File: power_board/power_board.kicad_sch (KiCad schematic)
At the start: 0 parts

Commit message: Added test point
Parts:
- added TP1: Test_Point, symbol URC:Test_Point
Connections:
- new net GND: TP1.1
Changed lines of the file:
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@@
 (kicad_sch (version 20230121) (generator eeschema)
   (paper "A4")
+  (wire (pts (xy 40.64 165.1) (xy 40.64 171.45))
+    (stroke (width 0) (type default))
+  )
+  (symbol (lib_id "URC:GND") (at 40.64 171.45 0) (unit 1)
+    (in_bom yes) (on_board yes) (dnp no) (fields_autoplaced)
+    (property "Reference" "#PWR01" (at 40.64 177.8 0)
+      (effects (font (size 1.27 1.27)) hide)
+    )
+    (property "Value" "GND" (at 40.64 176.53 0)
+      (effects (font (size 1.27 1.27)))
+    )
+    (property "Footprint" "" (at 40.64 171.45 0)
+      (effects (font (size 1.27 1.27)) hide)
+    )
+    (property "Datasheet" "" (at 40.64 171.45 0)
+      (effects (font (size 1.27 1.27)) hide)
+    )
+    (pin "1")
+    (instances
+      (project "power_board"
+        (path "/8fb9e798-2690-4afb-a1e7-64efc74d0eca"
+          (reference "#PWR01") (unit 1)
+        )
+      )
+    )
+  )
+  (symbol (lib_id "URC:Test_Point") (at 40.64 165.1 0) (unit 1)
+    (in_bom yes) (on_board yes) (dnp no) (fields_autoplaced)
+    (property "Reference" "TP1" (at 43.18 160.528 0)
+      (effects (font (size 1.27 1.27)) (justify left))
+    )
+    (property "Value" "Test_Point" (at 43.18 163.068 0)
+      (effects (font (size 1.27 1.27)) (justify left))
+    )
+    (property "Footprint" "" (at 45.72 165.1 0)
+      (effects (font (size 1.27 1.27)) hide)
+    )
+    (property "Datasheet" "~" (at 45.72 165.1 0)
+      (effects (font (size 1.27 1.27)) hide)
+    )
+    (pin "1")
+    (instances
+      (project "power_board"
+        (path "/8fb9e798-2690-4afb-a1e7-64efc74d0eca"
+          (reference "TP1") (unit 1)
+        )
+      )
+    )
+  )
   (sheet_instances
     (path "/" (page "1"))

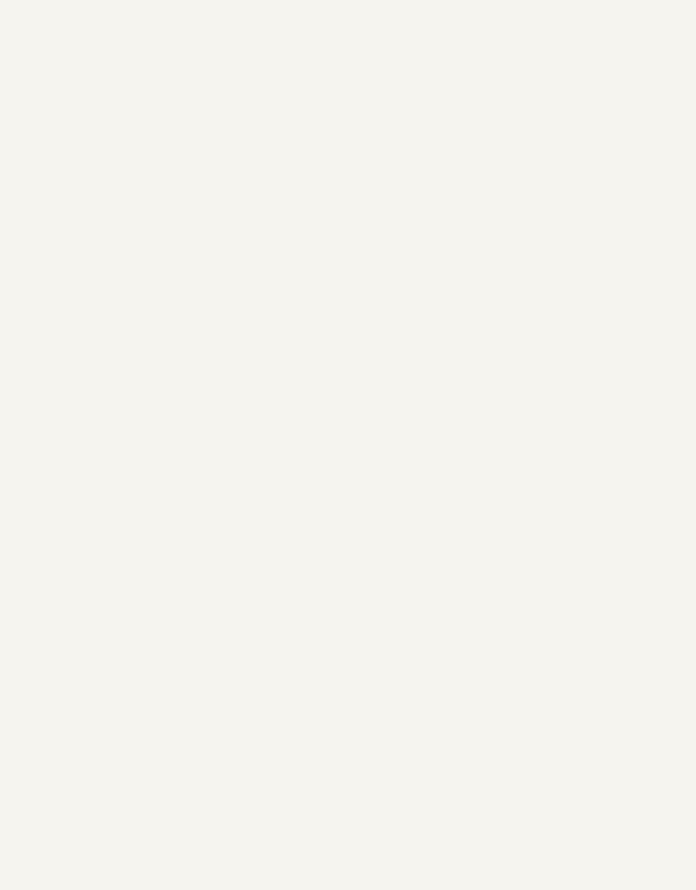
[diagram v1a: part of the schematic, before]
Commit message: Modified LCD Display symbol, added Arduino and LCD Display to schematic
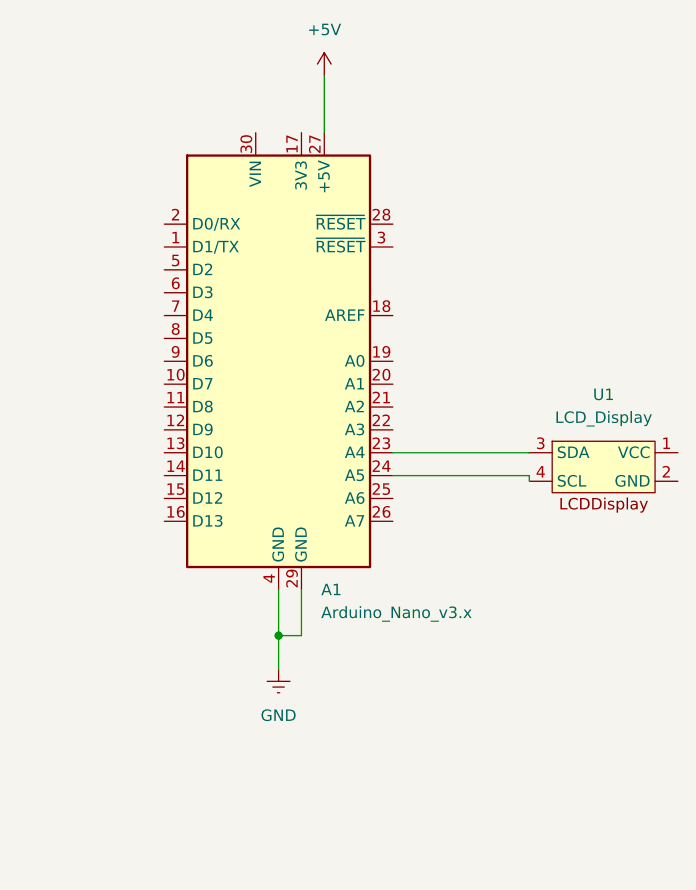
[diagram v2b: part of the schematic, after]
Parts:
- added A1: Arduino_Nano_v3.x, Module:Arduino_Nano, symbol URC:Arduino_Nano_v3.x
- added U1: LCD_Display, symbol URC:LCD_Display
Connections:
- net GND: now also A1.29 (GND), A1.4 (GND)
- new net: A1.23 (A4), U1.3 (SDA)
- new net: A1.24 (A5), U1.4 (SCL)
- new net +5V: A1.27 (+5V)
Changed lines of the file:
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@@
 (kicad_sch (version 20230121) (generator eeschema)
   (paper "A4")
+  (junction (at 142.24 104.14) (diameter 0) (color 0 0 0 0)
+  )
+  (wire (pts (xy 142.24 104.14) (xy 142.24 107.95))
+    (stroke (width 0) (type default))
+  )
+  (wire (pts (xy 170.1009 83.82) (xy 170.1009 83.815))
+    (stroke (width 0) (type default))
+  )
+  (wire (pts (xy 154.94 83.82) (xy 170.1009 83.82))
+    (stroke (width 0) (type default))
+  )
+  (wire (pts (xy 147.32 41.91) (xy 147.32 48.26))
+    (stroke (width 0) (type default))
+  )
+  (wire (pts (xy 170.1009 86.36) (xy 170.1009 86.99))
+    (stroke (width 0) (type default))
+  )
   (wire (pts (xy 40.64 165.1) (xy 40.64 171.45))
     (stroke (width 0) (type default))
   )
+  (wire (pts (xy 142.24 104.14) (xy 144.78 104.14))
+    (stroke (width 0) (type default))
+  )
+  (wire (pts (xy 142.24 99.06) (xy 142.24 104.14))
+    (stroke (width 0) (type default))
+  )
+  (wire (pts (xy 144.78 99.06) (xy 144.78 104.14))
+    (stroke (width 0) (type default))
+  )
+  (wire (pts (xy 154.94 86.36) (xy 170.1009 86.36))
+    (stroke (width 0) (type default))
+  )
+  (symbol (lib_id "URC:LCD_Display") (at 178.3559 81.91 0) (unit 1)
+    (in_bom yes) (on_board yes) (dnp no) (fields_autoplaced)
+    (property "Reference" "U1" (at 178.3559 77.3765 0)
+      (effects (font (size 1.27 1.27)))
+    )
+    (property "Value" "LCD_Display" (at 178.3559 79.9165 0)
+      (effects (font (size 1.27 1.27)))
+    )
+    (property "Footprint" "" (at 178.3559 81.91 0)
+      (effects (font (size 1.27 1.27)) hide)
+    )
+    (property "Datasheet" "" (at 178.3559 81.91 0)
+      (effects (font (size 1.27 1.27)) hide)
+    )
+    (pin "1")
+    (pin "2")
+    (pin "3")
+    (pin "4")
+    (instances
+      (project "power_board"
+        (path "/8fb9e798-2690-4afb-a1e7-64efc74d0eca"
+          (reference "U1") (unit 1)
+        )
+      )
+    )
+  )
   (symbol (lib_id "URC:GND") (at 40.64 171.45 0) (unit 1)
     (in_bom yes) (on_board yes) (dnp no) (fields_autoplaced)
@@
     )
   )
+  (symbol (lib_id "URC:Arduino_Nano_v3.x") (at 142.24 73.66 0) (unit 1)
+    (in_bom yes) (on_board yes) (dnp no) (fields_autoplaced)
+    (property "Reference" "A1" (at 146.9741 99.06 0)
+      (effects (font (size 1.27 1.27)) (justify left))
+    )
+    (property "Value" "Arduino_Nano_v3.x" (at 146.9741 101.6 0)
+      (effects (font (size 1.27 1.27)) (justify left))
+    )
+    (property "Footprint" "Module:Arduino_Nano" (at 142.24 73.66 0)
+      (effects (font (size 1.27 1.27) italic) hide)
+    )
+    (property "Datasheet" "http://www.mouser.com/pdfdocs/Gravitech_Arduino_Nano3_0.pdf" (at 142.24 73.66 0)
+      (effects (font (size 1.27 1.27)) hide)
+    )
+    (pin "1")
+    (pin "10")
+    (pin "11")
+    (pin "12")
+    (pin "13")
+    (pin "14")
+    (pin "15")
+    (pin "16")
+    (pin "17")
+    (pin "18")
+    (pin "19")
+    (pin "2")
+    (pin "20")
+    (pin "21")
+    (pin "22")
+    (pin "23")
+    (pin "24")
+    (pin "25")
+    (pin "26")
+    (pin "27")
+    (pin "28")
+    (pin "29")
+    (pin "3")
+    (pin "30")
+    (pin "4")
+    (pin "5")
+    (pin "6")
+    (pin "7")
+    (pin "8")
+    (pin "9")
+    (instances
+      (project "power_board"
+        (path "/8fb9e798-2690-4afb-a1e7-64efc74d0eca"
+          (reference "A1") (unit 1)
+        )
+      )
+    )
+  )
   (symbol (lib_id "URC:Test_Point") (at 40.64 165.1 0) (unit 1)
     (in_bom yes) (on_board yes) (dnp no) (fields_autoplaced)
@@
         )
       )
+    )
+  )
+  (symbol (lib_id "URC:GND") (at 142.24 107.95 0) (unit 1)
+    (in_bom yes) (on_board yes) (dnp no) (fields_autoplaced)
+    (property "Reference" "#PWR03" (at 142.24 114.3 0)
+      (effects (font (size 1.27 1.27)) hide)
+    )
+    (property "Value" "GND" (at 142.24 113.03 0)
+      (effects (font (size 1.27 1.27)))
+    )
+    (property "Footprint" "" (at 142.24 107.95 0)
+      (effects (font (size 1.27 1.27)) hide)
+    )
+    (property "Datasheet" "" (at 142.24 107.95 0)
+      (effects (font (size 1.27 1.27)) hide)
+    )
+    (pin "1")
+    (instances
+      (project "power_board"
+        (path "/8fb9e798-2690-4afb-a1e7-64efc74d0eca"
+          (reference "#PWR03") (unit 1)
+        )
+      )
+    )
+  )
+  (symbol (lib_id "URC:+5V") (at 147.32 41.91 0) (unit 1)
+    (in_bom yes) (on_board yes) (dnp no) (fields_autoplaced)
+    (property "Reference" "#PWR02" (at 147.32 45.72 0)
+      (effects (font (size 1.27 1.27)) hide)
+    )
+    (property "Value" "+5V" (at 147.32 36.83 0)
+      (effects (font (size 1.27 1.27)))
+    )
+    (property "Footprint" "" (at 147.32 41.91 0)
+      (effects (font (size 1.27 1.27)) hide)
+    )
+    (property "Datasheet" "" (at 147.32 41.91 0)
+      (effects (font (size 1.27 1.27)) hide)
+    )
+    (pin "1")
+    (instances
+      (project "power_board"
+        (path "/8fb9e798-2690-4afb-a1e7-64efc74d0eca"
+          (reference "#PWR02") (unit 1)
+        )
+      )

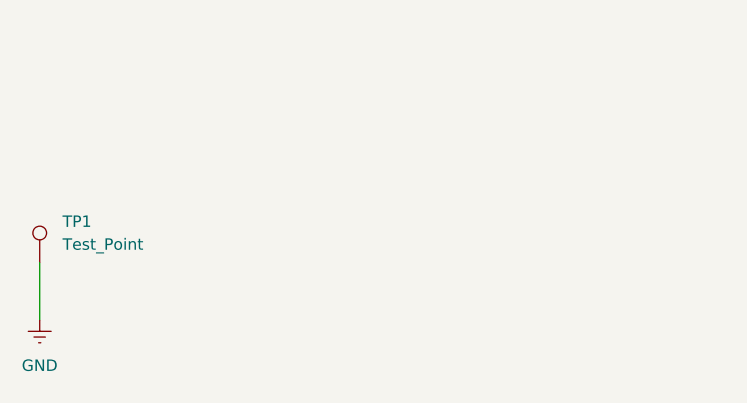
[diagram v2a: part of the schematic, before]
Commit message: TP2 and TP3 added
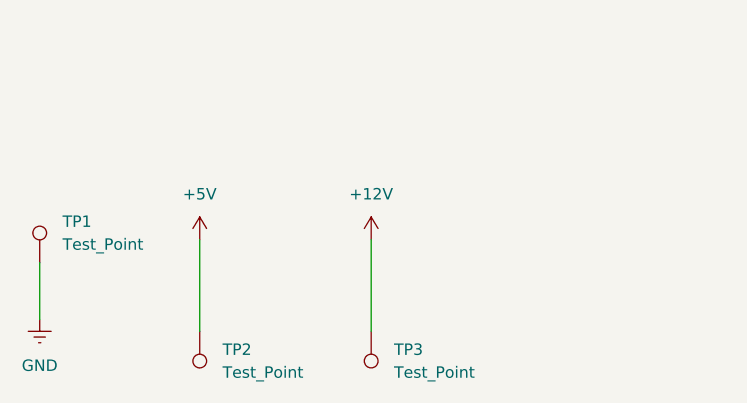
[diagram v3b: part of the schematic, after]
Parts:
- added TP2, TP3: Test_Point, symbol URC:Test_Point
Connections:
- net +5V: now also TP2.1
- new net +12V: TP3.1

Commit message: Fixed display
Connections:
- net GND: now also U1.2 (GND)
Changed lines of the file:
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@@
+	(wire
+		(pts
+			(xy 186.6109 86.99) (xy 186.6109 86.9558)
+		)
+		(stroke
+			(width 0)
+			(type default)
+		)
+	)
 	(wire
 		(pts
@@
 	(wire
 		(pts
+			(xy 186.69 83.82) (xy 193.04 83.82)
+		)
+		(stroke
+			(width 0)
+			(type default)
+		)
+	)
+	(wire
+		(pts
 			(xy 77.47 162.56) (xy 77.47 172.72)
 		)
@@
 	(wire
 		(pts
+			(xy 193.04 86.9558) (xy 193.04 90.17)
+		)
+		(stroke
+			(width 0)
+			(type default)
+		)
+	)
+	(wire
+		(pts
 			(xy 142.24 104.14) (xy 144.78 104.14)
+		)
+		(stroke
+			(width 0)
+			(type default)
+		)
+	)
+	(wire
+		(pts
+			(xy 186.6109 86.9558) (xy 193.04 86.9558)
 		)
 		(stroke
@@
 	)
 	(symbol
+		(lib_id "URC:GND")
+		(at 193.04 90.17 0)
+		(unit 1)
+		(exclude_from_sim no)
+		(in_bom yes)
+		(on_board yes)
+		(dnp no)
+		(fields_autoplaced yes)
+		(property "Reference" "#PWR07"
+			(at 193.04 96.52 0)
+			(effects
+				(font
+					(size 1.27 1.27)
+				)
+				(hide yes)
+			)
+		)
+		(property "Value" "GND"
+			(at 193.04 95.25 0)
+			(effects
+				(font
+					(size 1.27 1.27)
+				)
+			)
+		)
+		(property "Footprint" ""
+			(at 193.04 90.17 0)
+			(effects
+				(font
+					(size 1.27 1.27)
+				)
+				(hide yes)
+			)
+		)
+		(property "Datasheet" ""
+			(at 193.04 90.17 0)
+			(effects
+				(font
+					(size 1.27 1.27)
+				)
+				(hide yes)
+			)
+		)
+		(property "Description" "Power symbol creates a global label with name \"GNDREF\" , reference supply ground"
+			(at 193.04 90.17 0)
+			(effects
+				(font
+					(size 1.27 1.27)
+				)
+				(hide yes)
+			)
+		)
+		(pin "1"
+		)
+		(instances
+			(project ""
+				(path "/8fb9e798-2690-4afb-a1e7-64efc74d0eca"
+					(reference "#PWR07")
+					(unit 1)
+				)
+			)
+		)
+	)
+	(symbol
 		(lib_id "URC:Arduino_Nano_v3.x")
 		(at 142.24 73.66 0)
@@
 					(unit 1)
 				)
+			)
+		)
+	)
+	(symbol
+		(lib_id "URC:+5V")
+		(at 193.04 83.82 270)
+		(unit 1)
+		(exclude_from_sim no)
+		(in_bom yes)
+		(on_board yes)
+		(dnp no)
+		(fields_autoplaced yes)
+		(property "Reference" "#PWR06"
+			(at 189.23 83.82 0)
+			(effects
+				(font
+					(size 1.27 1.27)
+				)
+				(hide yes)
+			)
+		)
+		(property "Value" "+5V"
+			(at 196.85 83.8199 90)
+			(effects
+				(font
+					(size 1.27 1.27)
+				)
+				(justify left)
+			)
+		)
+		(property "Footprint" ""
+			(at 193.04 83.82 0)
+			(effects
+				(font
+					(size 1.27 1.27)
+				)
+				(hide yes)
+			)
+		)
+		(property "Datasheet" ""
+			(at 193.04 83.82 0)
+			(effects
+				(font
+					(size 1.27 1.27)
+				)
+				(hide yes)
+			)
+		)
+		(property "Description" "Power symbol creates a global label with name \"+5V\""
+			(at 193.04 83.82 0)
+			(effects
+				(font
+					(size 1.27 1.27)
+				)
+				(hide yes)
+			)
+		)
+		(pin "1"
+		)
+		(instances
+			(project ""
+				(path "/8fb9e798-2690-4afb-a1e7-64efc74d0eca"
+					(reference "#PWR06")
+					(unit 1)
+				)

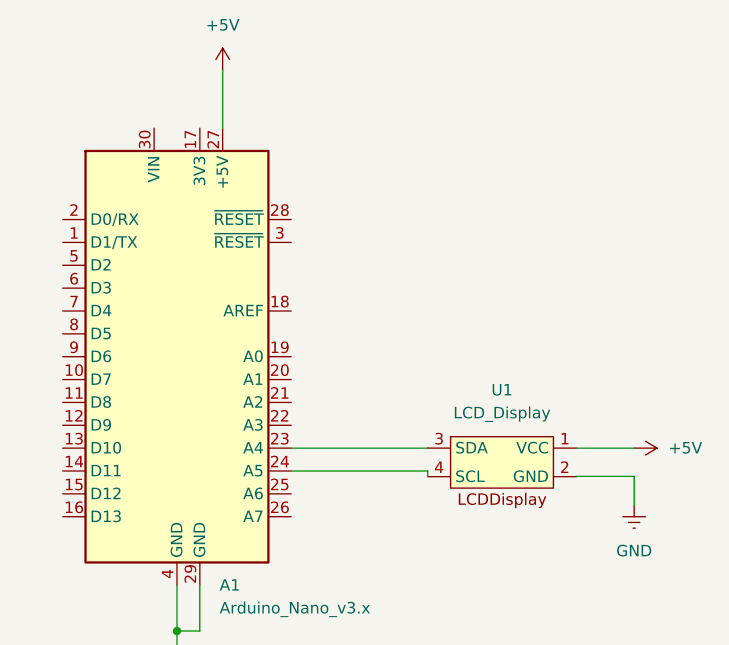
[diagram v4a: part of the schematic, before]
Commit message: Added R1, R2
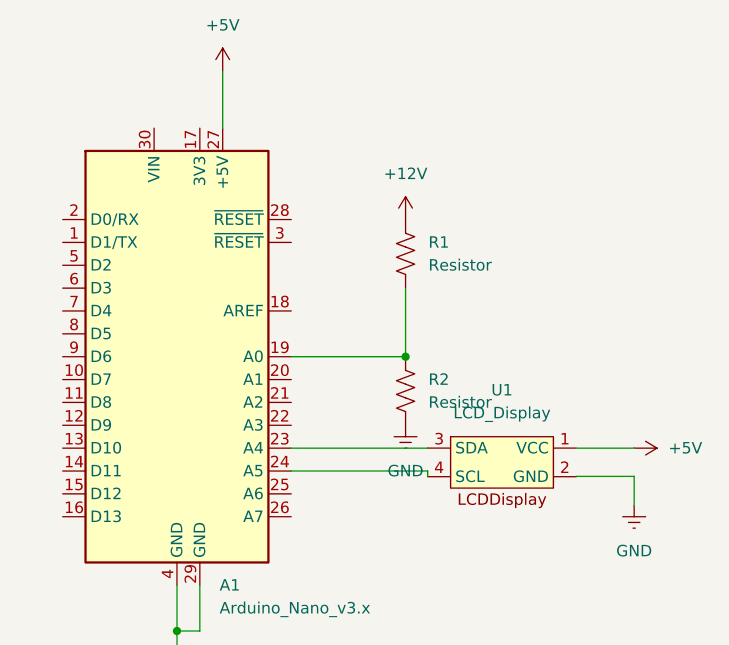
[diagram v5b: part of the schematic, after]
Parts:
- added R1, R2: Resistor, symbol URC:Resistor
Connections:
- net +12V: now also R1.1
- net GND: now also R2.2
- net at A1.19 (A0): now also R1.2, R2.1

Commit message: power switch
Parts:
- added C1: Capacitor, symbol URC:Capacitor
- added F1: Fuse, symbol URC:Fuse
- added J1: 2_Pin_Connector, symbol URC:2_Pin_Connector
- added SW1: Switch, symbol URC:Switch
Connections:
- net +12V: now also F1.2
- net GND: now also C1.2, J1.2 (Pin_2)
- new net: C1.1, J1.1 (Pin_1), SW1.1 (A)
- new net: F1.1, SW1.2 (B)

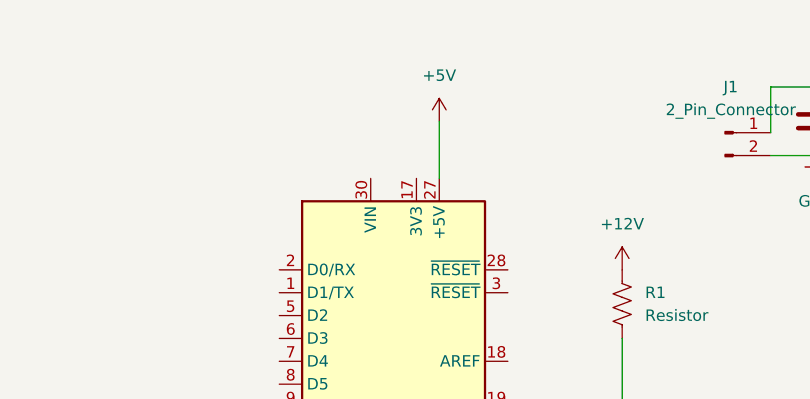
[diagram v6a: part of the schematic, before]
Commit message: Fixed mistake on Arduino
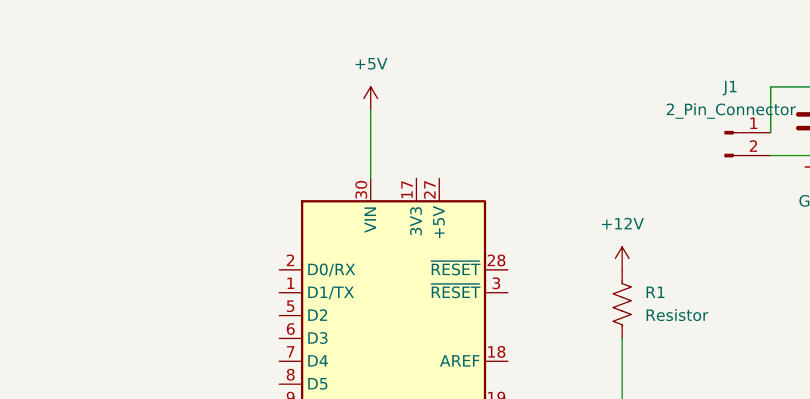
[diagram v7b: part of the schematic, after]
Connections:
- net +5V: now also A1.30 (VIN); no longer A1.27 (+5V)
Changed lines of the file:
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@@
 	(wire
 		(pts
-			(xy 147.32 41.91) (xy 147.32 48.26)
+			(xy 184.15 43.18) (xy 184.15 38.1)
 		)
 		(stroke
@@
 	(wire
 		(pts
-			(xy 184.15 43.18) (xy 184.15 38.1)
+			(xy 170.1009 86.36) (xy 170.1009 86.99)
 		)
 		(stroke
@@
 	(wire
 		(pts
-			(xy 170.1009 86.36) (xy 170.1009 86.99)
+			(xy 186.69 83.82) (xy 193.04 83.82)
 		)
 		(stroke
@@
 	(wire
 		(pts
-			(xy 186.69 83.82) (xy 193.04 83.82)
+			(xy 77.47 162.56) (xy 77.47 172.72)
 		)
 		(stroke
@@
 	(wire
 		(pts
-			(xy 77.47 162.56) (xy 77.47 172.72)
+			(xy 40.64 165.1) (xy 40.64 171.45)
 		)
 		(stroke
@@
 	(wire
 		(pts
-			(xy 40.64 165.1) (xy 40.64 171.45)
+			(xy 58.42 162.56) (xy 58.42 172.72)
 		)
 		(stroke
@@
 	(wire
 		(pts
-			(xy 58.42 162.56) (xy 58.42 172.72)
+			(xy 193.04 86.9558) (xy 193.04 90.17)
 		)
 		(stroke
@@
 	(wire
 		(pts
-			(xy 193.04 86.9558) (xy 193.04 90.17)
+			(xy 142.24 104.14) (xy 144.78 104.14)
 		)
 		(stroke
@@
 	(wire
 		(pts
-			(xy 142.24 104.14) (xy 144.78 104.14)
+			(xy 184.15 45.72) (xy 189.23 45.72)
 		)
 		(stroke
@@
 	(wire
 		(pts
-			(xy 184.15 45.72) (xy 189.23 45.72)
+			(xy 139.7 40.64) (xy 139.7 48.26)
 		)
 		(stroke
@@
 	(symbol
 		(lib_id "URC:+5V")
-		(at 147.32 41.91 0)
+		(at 139.7 40.64 0)
 		(unit 1)
 		(exclude_from_sim no)
@@
 		(fields_autoplaced yes)
 		(property "Reference" "#PWR02"
-			(at 147.32 45.72 0)
+			(at 139.7 44.45 0)
 			(effects
 				(font
@@
 		)
 		(property "Value" "+5V"
-			(at 147.32 36.83 0)
-			(effects
-				(font
-					(size 1.27 1.27)
-				)
-			)
-		)
-		(property "Footprint" ""
-			(at 147.32 41.91 0)
+			(at 139.7 35.56 0)
+			(effects
+				(font
+					(size 1.27 1.27)
+				)
+			)
+		)
+		(property "Footprint" ""
+			(at 139.7 40.64 0)
 			(effects
 				(font
@@
 		)
 		(property "Datasheet" ""
-			(at 147.32 41.91 0)
+			(at 139.7 40.64 0)
 			(effects
 				(font
@@
 		)
 		(property "Description" ""
-			(at 147.32 41.91 0)
-			(effects
-				(font
+			(at 139.7 40.64 0)
+			(effects
+				(font

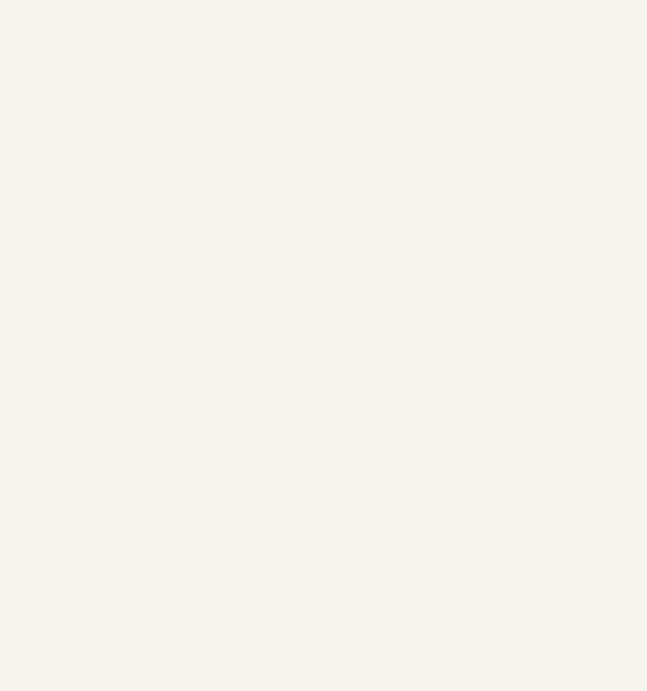
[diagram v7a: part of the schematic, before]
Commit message: U1
added U1 to schematic
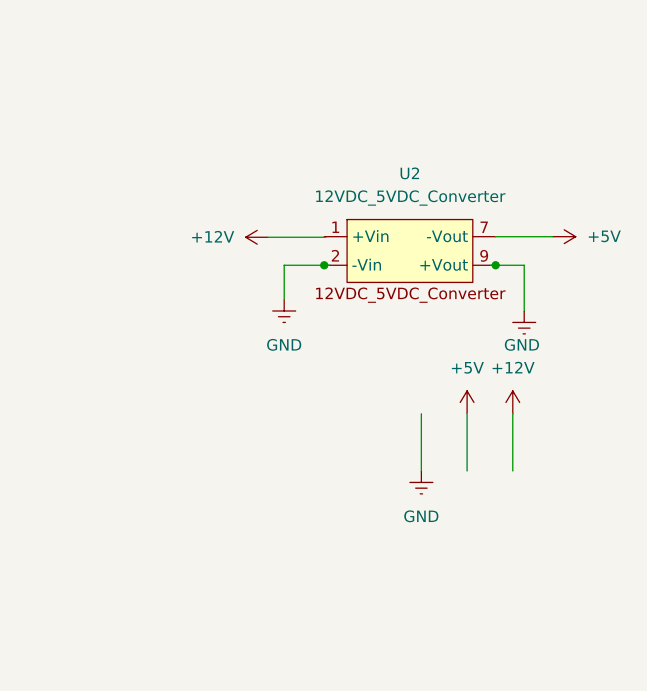
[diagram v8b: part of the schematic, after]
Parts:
- added U2: 12VDC_5VDC_Converter, symbol URC:12VDC_5VDC_Converter
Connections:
- net +5V: now also U2.7 (-Vout)
- net GND: now also U2.2 (-Vin), U2.9 (+Vout)
